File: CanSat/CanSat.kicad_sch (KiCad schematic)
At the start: 7 parts, among them J1 MPU_XH2.54_M, J2 MPU_XH2.54_H, U1 ESP32_DevKit_V1, U2 LoRa Ra-02, U3 NEO6MV2 GPS, U4 MPU-6050, U5 BME280

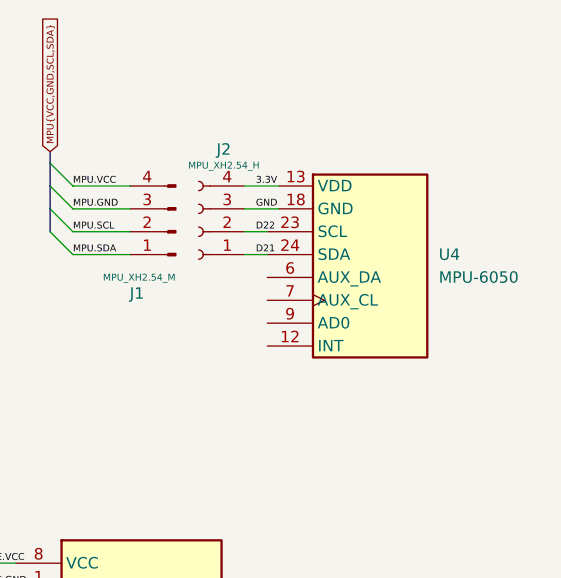
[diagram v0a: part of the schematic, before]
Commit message: Updated schematic and added footprints
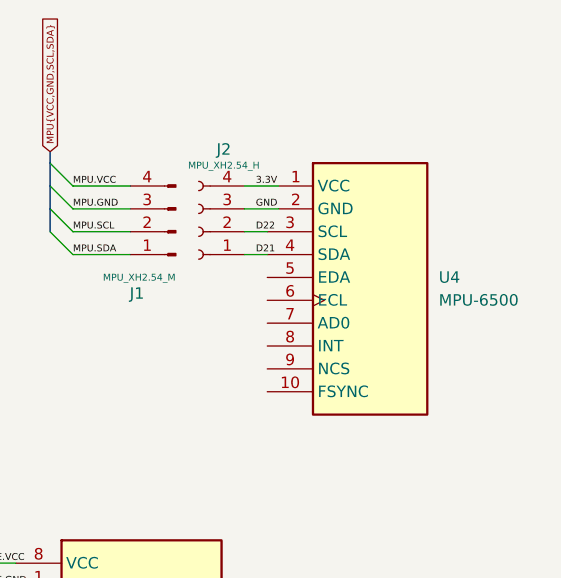
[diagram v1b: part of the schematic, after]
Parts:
- removed U4: MPU-6050, Connector_PinSocket_2.54mm:PinSocket_1x08_P2.54mm_Vertical, symbol MyLibrary:MPU-6050
- added U4: MPU-6500, symbol MyLibrary:MPU-6500
- U2: footprint Connector_PinHeader_2.54mm:PinHeader_2x08_P2.54mm_Vertical -> MyLibrary:LoRa Ra-02
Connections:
- net 3.3V: now also U4.1 (VCC)
- net D21: now also U4.4 (SDA)
- net D22: now also U4.3 (SCL)
- net GND: now also U4.2 (GND)
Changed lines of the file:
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@@
+	)
+	(symbol
+		(lib_id "MyLibrary:MPU-6500")
+		(at 116.84 132.08 0)
+		(unit 1)
+		(exclude_from_sim no)
+		(in_bom yes)
+		(on_board yes)
+		(dnp no)
+		(fields_autoplaced yes)
+		(property "Reference" "U4"
+			(at 124.46 130.8099 0)
+			(effects
+				(font
+					(size 1.27 1.27)
+				)
+				(justify left)
+			)
+		)
+		(property "Value" "MPU-6500"
+			(at 124.46 133.3499 0)
+			(effects
+				(font
+					(size 1.27 1.27)
+				)
+				(justify left)
+			)
+		)
+		(property "Footprint" ""
+			(at 116.84 132.08 0)
+			(effects
+				(font
+					(size 1.27 1.27)
+				)
+				(hide yes)
+			)
+		)
+		(property "Datasheet" ""
+			(at 116.84 132.08 0)
+			(effects
+				(font
+					(size 1.27 1.27)
+				)
+				(hide yes)
+			)
+		)
+		(property "Description" ""
+			(at 116.84 132.08 0)
+			(effects
+				(font
+					(size 1.27 1.27)
+				)
+				(hide yes)
+			)
+		)
+		(pin "4"
+		)
+		(pin "3"
+		)
+		(pin "5"
+		)
+		(pin "6"
+		)
+		(pin "9"
+		)
+		(pin "2"
+		)
+		(pin "1"
+		)
+		(pin "7"
+		)
+		(pin "10"
+		)
+		(pin "8"
+		)
+		(instances
+			(project ""
+				(path "/ad8e5941-aa23-4687-a9fe-71094ed41176"
+					(reference "U4")
+					(unit 1)
+				)
+			)
+		)
 	)
 	(symbol
@@
 			)
 		)
-		(property "Footprint" "Connector_PinHeader_2.54mm:PinHeader_2x08_P2.54mm_Vertical"
+		(property "Footprint" "MyLibrary:LoRa Ra-02"
 			(at 45.72 130.81 0)
 			(effects
@@
 					(unit 1)
 				)
-			)
-		)
-	)
-	(symbol
-		(lib_id "MyLibrary:MPU-6050")
-		(at 116.84 129.54 0)
-		(unit 1)
-		(exclude_from_sim no)
-		(in_bom yes)
-		(on_board yes)
-		(dnp no)
-		(fields_autoplaced yes)
-		(property "Reference" "U4"
-			(at 124.46 128.2699 0)
-			(effects
-				(font
-					(size 1.27 1.27)
-				)
-				(justify left)
-			)
-		)
-		(property "Value" "MPU-6050"
-			(at 124.46 130.8099 0)
-			(effects
-				(font
-					(size 1.27 1.27)
-				)
-				(justify left)
-			)
-		)
-		(property "Footprint" "Connector_PinSocket_2.54mm:PinSocket_1x08_P2.54mm_Vertical"
-			(at 116.84 149.86 0)
-			(effects
-				(font
-					(size 1.27 1.27)
-				)
-				(hide yes)
-			)
-		)
-		(property "Datasheet" "https://invensense.tdk.com/wp-content/uploads/2015/02/MPU-6000-Datasheet1.pdf"
-			(at 117.856 154.94 0)
-			(effects
-				(font
-					(size 1.27 1.27)
-				)
-				(hide yes)
-			)
-		)
-		(property "Description" "InvenSense 6-Axis Motion Sensor, Gyroscope, Accelerometer, I2C"
-			(at 117.602 152.908 0)
-			(effects
-				(font
-					(size 1.27 1.27)
-				)
-				(hide yes)
-			)
-		)
-		(pin "7"
-		)
-		(pin "12"
-		)
-		(pin "24"
-		)
-		(pin "6"
-		)
-		(pin "23"
-		)
-		(pin "18"
-		)
-		(pin "9"
-		)
-		(pin "13"
-		)
-		(instances
-			(project ""
-				(path "/ad8e5941-aa23-4687-a9fe-71094ed41176"
-					(reference "U4")
-					(unit 1)
-				)

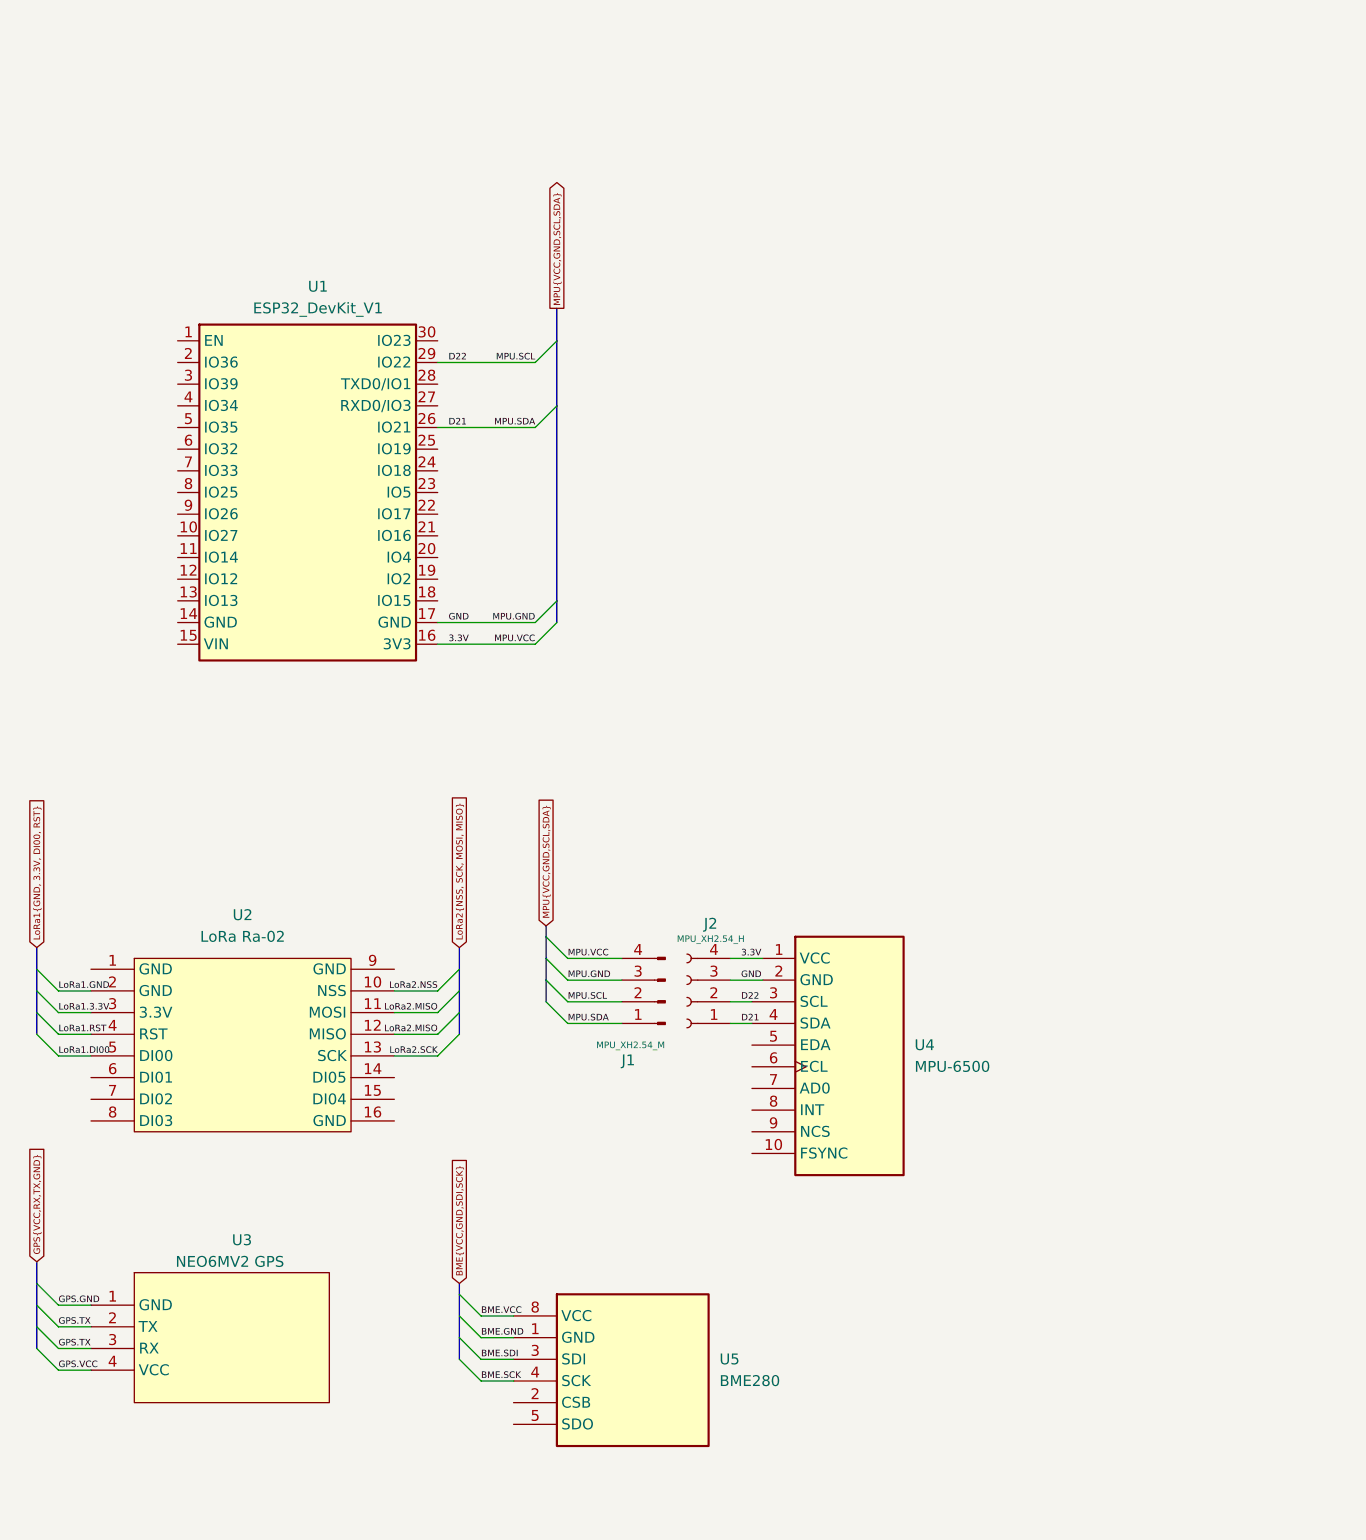
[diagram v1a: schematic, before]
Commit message: Change schemes and footprints
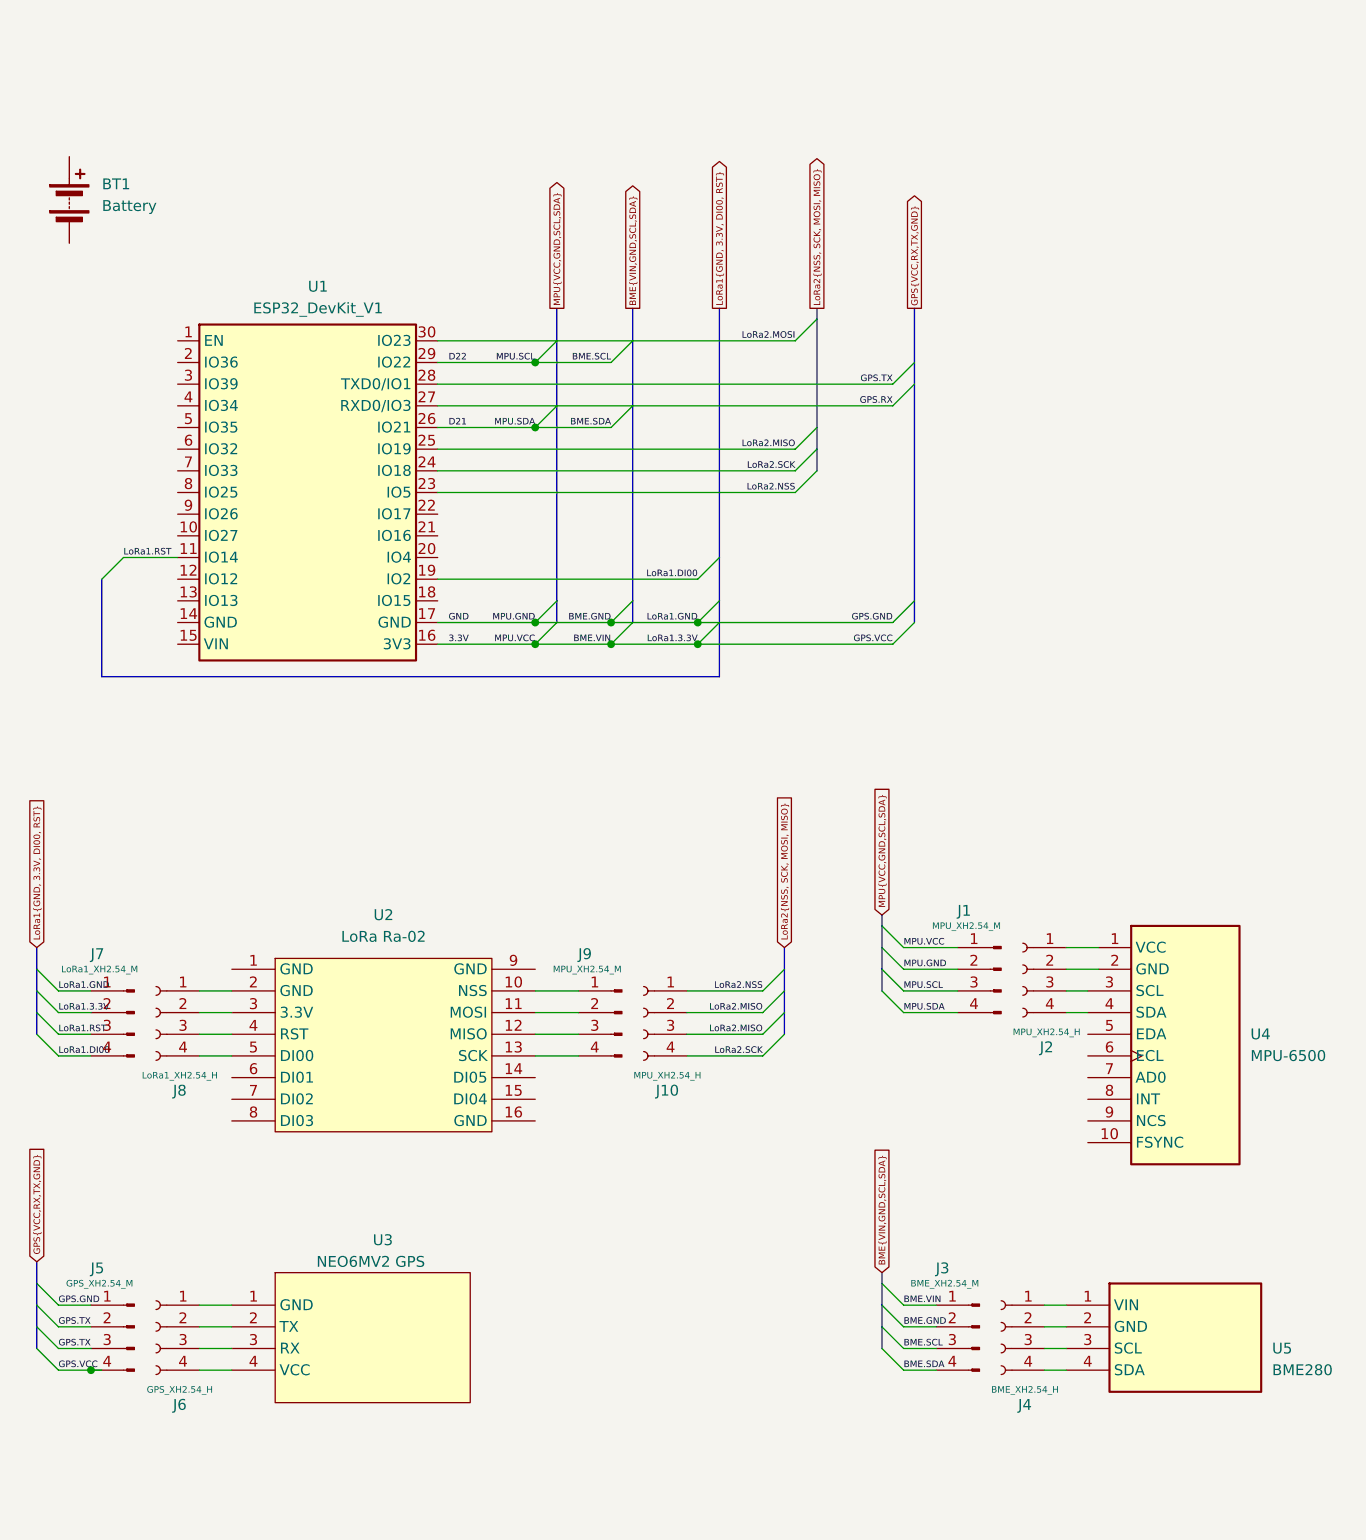
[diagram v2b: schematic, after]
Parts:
- added BT1: Battery, symbol Device:Battery
- added J10: MPU_XH2.54_H, Connector_JST:JST_XH_B4B-XH-A_1x04_P2.50mm_Vertical, symbol Connector:Conn_01x04_Socket
- added J3: BME_XH2.54_M, Connector_JST:JST_XH_B4B-XH-A_1x04_P2.50mm_Vertical, symbol Connector:Conn_01x04_Pin
- added J4: BME_XH2.54_H, Connector_JST:JST_XH_B4B-XH-A_1x04_P2.50mm_Vertical, symbol Connector:Conn_01x04_Socket
- added J5: GPS_XH2.54_M, Connector_JST:JST_XH_B4B-XH-A_1x04_P2.50mm_Vertical, symbol Connector:Conn_01x04_Pin
- added J6: GPS_XH2.54_H, Connector_JST:JST_XH_B4B-XH-A_1x04_P2.50mm_Vertical, symbol Connector:Conn_01x04_Socket
- added J7: LoRa1_XH2.54_M, Connector_JST:JST_XH_B4B-XH-A_1x04_P2.50mm_Vertical, symbol Connector:Conn_01x04_Pin
- added J8: LoRa1_XH2.54_H, Connector_JST:JST_XH_B4B-XH-A_1x04_P2.50mm_Vertical, symbol Connector:Conn_01x04_Socket
- added J9: MPU_XH2.54_M, Connector_JST:JST_XH_B4B-XH-A_1x04_P2.50mm_Vertical, symbol Connector:Conn_01x04_Pin
- U3: footprint Connector_PinHeader_2.54mm:PinHeader_1x04_P2.54mm_Vertical -> MyLibrary:NE06MV2 GPS
- U4: footprint (none) -> MyLibrary:MPU-6500
- U5: footprint Connector_PinHeader_2.54mm:PinHeader_1x06_P2.54mm_Vertical -> MyLibrary:BME280
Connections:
- net 3.3V: now also J1.1 (Pin_1), J3.1 (Pin_1), J5.4 (Pin_4), J7.2 (Pin_2); no longer J1.4 (Pin_4), J2.4 (Pin_4), U4.1 (VCC)
- net BME.GND: now also J1.2 (Pin_2), U1.17 (GND), J3.2 (Pin_2), J5.1 (Pin_1), J7.1 (Pin_1); no longer U5.1 (GND)
- net GPS.TX: now also U1.28 (TXD0/IO1), J5.2 (Pin_2), J5.3 (Pin_3); no longer U3.2 (TX), U3.3 (RX)
- net LoRa1.DI00: now also U1.19 (IO2), J7.4 (Pin_4); no longer U2.5 (DI00)
- net LoRa1.RST: now also U1.11 (IO14), J7.3 (Pin_3); no longer U2.4 (RST)
- net LoRa2.MISO: now also U1.25 (IO19), J10.2 (Pin_2), J10.3 (Pin_3); no longer U2.11 (MOSI), U2.12 (MISO)
- net LoRa2.NSS: now also U1.23 (IO5), J10.1 (Pin_1); no longer U2.10 (NSS)
- net LoRa2.SCK: now also U1.24 (IO18), J10.4 (Pin_4); no longer U2.13 (SCK)
- net at U5.2 (GND): now also J4.2 (Pin_2)
- net GPS.RX: now reaches U1.27 (RXD0/IO3)
- net LoRa2.MOSI: now reaches U1.30 (IO23)
- net BME.SCK: no longer names the net of U5.4 (SDA)
- net BME.SCK: now also J4.4 (Pin_4)
- net BME.SDI: no longer names the net of U5.3 (SCL)
- net BME.SDI: now also J4.3 (Pin_3)
- removed net BME.VCC: U5.8 (VCC)
- removed net D21: J1.1 (Pin_1), J2.1 (Pin_1), U1.26 (IO21), U4.4 (SDA)
- removed net D22: J1.2 (Pin_2), J2.2 (Pin_2), U1.29 (IO22), U4.3 (SCL)
- removed net GND: J1.3 (Pin_3), J2.3 (Pin_3), U1.17 (GND), U4.2 (GND)
- net GPS.GND: no longer names the net of U3.1 (GND)
- net GPS.GND: now also J6.1 (Pin_1)
- net GPS.VCC: no longer names the net of U3.4 (VCC)
- net GPS.VCC: now also J6.4 (Pin_4)
- net LoRa1.3.3V: no longer names the net of U2.3 (3.3V)
- net LoRa1.3.3V: now also J8.2 (Pin_2)
- net LoRa1.GND: no longer names the net of U2.2 (GND)
- net LoRa1.GND: now also J8.1 (Pin_1)
- new net: J4.1 (Pin_1), U5.1 (VIN)
- new net: J9.1 (Pin_1), U2.10 (NSS)
- new net: J9.2 (Pin_2), U2.11 (MOSI)
- new net: J9.3 (Pin_3), U2.12 (MISO)
- new net: J9.4 (Pin_4), U2.13 (SCK)
- new net: J8.3 (Pin_3), U2.4 (RST)
- new net: J8.4 (Pin_4), U2.5 (DI00)
- new net: J6.2 (Pin_2), U3.2 (TX)
- new net: J6.3 (Pin_3), U3.3 (RX)
- new net: J2.1 (Pin_1), U4.1 (VCC)
- new net: J2.2 (Pin_2), U4.2 (GND)
- new net: J2.3 (Pin_3), U4.3 (SCL)
- new net: J2.4 (Pin_4), U4.4 (SDA)
- new net BME.SCL: J1.3 (Pin_3), J3.3 (Pin_3), U1.29 (IO22)
- new net BME.SDA: J1.4 (Pin_4), J3.4 (Pin_4), U1.26 (IO21)
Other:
- moved on the sheet: J1, J2, U2, U3, U4

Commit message: PCBv1
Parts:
- removed BT1: Battery, symbol Device:Battery
- added D1: LED_Testigo, Connector_JST:JST_XH_B2B-XH-A_1x02_P2.50mm_Vertical, symbol MyLibrary:LED_Red
- added J11: Battery_XH2.54_M, Connector_JST:JST_XH_B2B-XH-A_1x02_P2.50mm_Vertical, symbol Connector:Conn_01x02_Pin
- added J12: Battery_XH2.54_H, Connector_JST:JST_XH_B2B-XH-A_1x02_P2.50mm_Vertical, symbol Connector:Conn_01x02_Socket
- added J13: BatteryI2C_XH2.54_M, Connector_JST:JST_XH_B2B-XH-A_1x02_P2.50mm_Vertical, symbol Connector:Conn_01x02_Pin
- added J14: BatteryI2C_XH2.54_H, Connector_JST:JST_XH_B2B-XH-A_1x02_P2.50mm_Vertical, symbol Connector:Conn_01x02_Socket
- added R1: R_330Ohm, Resistor_THT:R_Axial_DIN0207_L6.3mm_D2.5mm_P7.62mm_Horizontal, symbol Device:R_US
- added SW1: SW_Power, Connector_JST:JST_XH_B2B-XH-A_1x02_P2.50mm_Vertical, symbol Switch:SW_Push
- added U6: LiPoBoostI2C, MyLibrary:LiPoBoostI2C, symbol MyLibrary:LiPoBoostI2C
- J10: value MPU_XH2.54_H -> LoRa2_XH2.54_H
- J9: value MPU_XH2.54_M -> LoRa2_XH2.54_M
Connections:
- net 3.3V: now also J5.1 (Pin_1), J7.1 (Pin_1); no longer J5.4 (Pin_4), J7.2 (Pin_2)
- net BME.GND: now also J5.2 (Pin_2), J7.2 (Pin_2); no longer J5.1 (Pin_1), J7.1 (Pin_1)
- net BME.SCL: now also J14.1 (Pin_1)
- net BME.SDA: now also J14.2 (Pin_2)
- net GPS.RX: now also J5.4 (Pin_4)
- net GPS.TX: no longer J5.2 (Pin_2)
- net LoRa2.MISO: no longer J10.2 (Pin_2)
- net LoRa2.MOSI: now also J10.4 (Pin_4)
- net LoRa2.SCK: now also J10.2 (Pin_2); no longer J10.4 (Pin_4)
- net at J9.2 (Pin_2): now also U2.13 (SCK); no longer U2.11 (MOSI)
- net at J9.4 (Pin_4): now also U2.11 (MOSI); no longer U2.13 (SCK)
- net at J8.1 (Pin_1): now also U2.3 (3.3V); no longer U2.2 (GND)
- net at J8.2 (Pin_2): now also U2.2 (GND); no longer U2.3 (3.3V)
- net at U3.1 (GND): now also J6.2 (Pin_2); no longer J6.1 (Pin_1)
- net at U3.2 (TX): now also J6.3 (Pin_3); no longer J6.2 (Pin_2)
- net at U3.3 (RX): now also J6.4 (Pin_4); no longer J6.3 (Pin_3)
- net at U3.4 (VCC): now also J6.1 (Pin_1); no longer J6.4 (Pin_4)
- net at U1.14 (GND): now also J12.1 (Pin_1)
- net at U1.15 (VIN): now also J12.2 (Pin_2)
- new net: J13.1 (Pin_1), U6.2 (SCL)
- new net: J13.2 (Pin_2), U6.1 (SDA)
- new net: J11.1 (Pin_1), R1.1, U6.3 (GND), U6.7 (GND)
- new net: SW1.2, U6.6 (VOUT)
- new net: D1.2 (A), J11.2 (Pin_2), SW1.1
- new net: D1.1 (K), R1.2
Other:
- moved on the sheet: J1, J10, J2, J3, J4, J5, J6, J7, J8, J9, U1, U2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
